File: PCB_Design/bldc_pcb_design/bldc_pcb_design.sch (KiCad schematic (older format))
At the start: 50 parts, among them IC1 DRV8305NPHPR, J1 Conn_01x04_Female, SW1 BOOT, SW2 RESET, U1 ESP32-WROOM-32D, U2 AS5600-ASOT, U3 LM2672M-3.3, U4 CSD18532NQ5B, U5 CSD18532NQ5B, U6 CSD18532NQ5B, U7 CSD18532NQ5B, U8 CSD18532NQ5B, U9 CSD18532NQ5B

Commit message: [Temp sensor] Added DS18S20Z+ and modified schematics
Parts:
- added C? (x2): 0.1uF, symbol Device:C
- added C? (x3): 2.2nF, symbol Device:C
- added D? (x2): LED, symbol Device:LED
- added R?: 4.7k, symbol Device:R
- added R?: 5k, symbol Device:R
- added R?: 330, symbol Device:R
- added U?: DS18S20Z+, SOIC127P600X175-8N, symbol DS18S20Z_:DS18S20Z+
- C11, C13, C9: value 1uF -> 0.01uF
- C14: value 4.7uF Ceramic -> 4.7uF
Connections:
- net labels added: TEMP_DQ
- net labels removed: +3V3
- wire segments 236 -> 261
- no-connect marks 5 -> 16
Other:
- note added: "**Confirm Usage of \nIO 5, 12, and 15 \n"
- note added: "3.3V Input Power LED\n"
- note added: "5-V internal analog \nsupply regulator\nbypass capacitor"
- note added: "Connect VDD to GND for\nParasite Power Mode:\nDeriving Power from DQ\nData line"
- note added: "Connect with-> \n3.3V or 5V, 50-mA LDO; \n connect 1-µF to GND\nReference voltage; \n LDO disabled"
- note added: "DQ - 1 Wire Line \nCommunication Interface\n"
- note added: "DQ - External Pull-Up"
- note added: "DRV_DVDD: 3.3V \ninternal digital\nsupply regulator"
- note added: "DRV_VREG: Internal\namplifier reference \nvoltage and SDO pullup."
- note added: "DRV_nFAULT: Fault\nIndicator and LED"
- note added: "High Side MOSFET Drain"
- note added: "PVDD: Power Bypass \nCapacitor and LED"
- note added: "PWRGD: Power Good DRV_VREG \nand MCU watchdog fault \nindication and LED"
- note added: "SNP1, SN2 and SN3 are negative current sense \ninput pins for amplifers 1,2 and 3 respectively\n"
- note added: "SO1, SO2 and SO3 are current amplifier output pins"
- note added: "SP1, SP2 and SP3 are positive current sense\ninput pins for amplifers 1,2 and 3 respectively\n"
- note added: "Temperature Sensor (DS18S20Z+)"
- note added: "VDRAIN Should \nHave Low\nImpedance Path\nTo Drain Of The \nHigh-Side FETs"
- note removed: "5-V internal analog supply \nregulator bypass capacitor"
- note removed: "Additional Circuitry"
- note removed: "Connect with-> \n3.3V or 5V, 50-mA LDO; \n connect 1-µF to GND\nReference voltage; LDO disabled"
- note removed: "DRV_DVDD: 3.3V internal digital\nsupply regulator"
- note removed: "DRV_VREG: Internalamplifier \nreference voltage and SDO pullup."
- note removed: "DRV_nFAULT: Fault\nIndicator"
- note removed: "High Side MOSFET\nDrain"
- note removed: "PWRGD: Power Good\nDRV_VREG and MCU \nwatchdog fault \nindication"
- note removed: "Power Bypass \nCapacitor"
- note removed: "Power LED\n"
- note removed: "SNP1, SN2 and SN3 are\nnegative current sense input pins\nfor amplifers 1,2 and 3 respectively\n"
- note removed: "SO1, SO2 and SO3 are \ncurrent amplifier output pins\n"
- note removed: "SP1, SP2 and SP3 are \npositive current sense input pins\nfor amplifers 1,2 and 3 respectively\n"
- moved on the sheet: C14, C15, C16, C17, C18, C19, C20, C21, C24, D3, R6, R7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

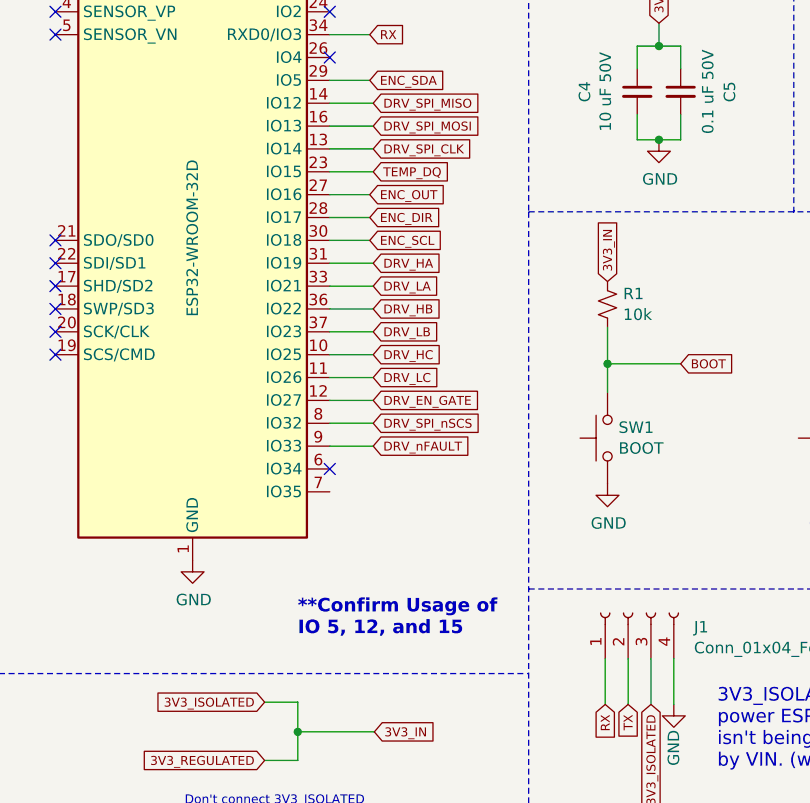
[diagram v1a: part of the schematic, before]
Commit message: Changed pin connections: IO34- DRV_nFAULT; IO15- NC; IO33- TEMP_DQ
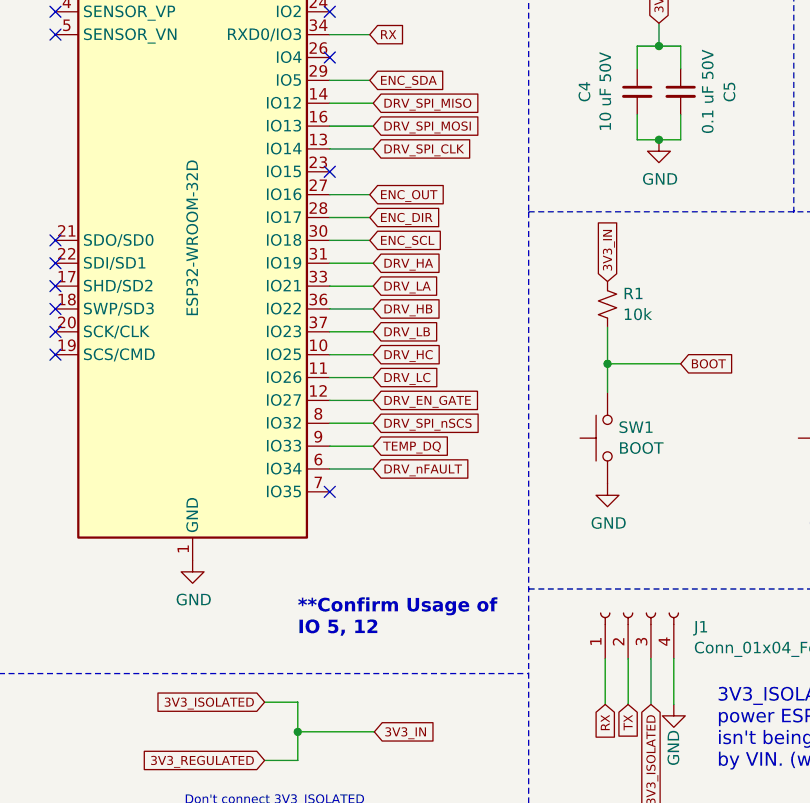
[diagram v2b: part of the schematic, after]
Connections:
- net DRV_nFAULT: now also U1.6 (IO34); no longer U1.9 (IO33)
- net TEMP_DQ: now also U1.9 (IO33); no longer U1.23 (IO15)
- no-connect marks 16 -> 17
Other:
- note added: "**Confirm Usage of \nIO 5, 12"
- note removed: "**Confirm Usage of \nIO 5, 12, and 15 \n"
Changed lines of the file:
@@
 Wire Wire Line
 	2290 2135 2100 2135
-Text GLabel 2290 3435 2    39   Input ~ 0
+Text GLabel 2290 3535 2    39   Input ~ 0
 DRV_nFAULT
 Text GLabel 2290 3135 2    39   Input ~ 0
@@
 	2290 3035 2100 3035
 Wire Wire Line
-	2290 3435 2100 3435
+	2290 3535 2100 3535
 Text GLabel 2290 2835 2    39   Input ~ 0
 DRV_HB
@@
 Wire Wire Line
 	8630 1155 8720 1155
-Text GLabel 2290 2235 2    39   Input ~ 0
+Text GLabel 2290 3435 2    39   Input ~ 0
 TEMP_DQ
 Wire Wire Line
-	2290 2235 2100 2235
+	2290 3435 2100 3435
 NoConn ~ 900  2535
 NoConn ~ 900  2635
@@
 NoConn ~ 2100 1735
 NoConn ~ 2100 1535
-NoConn ~ 2100 3535
+NoConn ~ 2100 3635
 $Comp
 L DS18S20Z_:DS18S20Z+ U?
@@
 	13770 3255 13770 2015
 Text Notes 1960 4270 0    59   ~ 12
-**Confirm Usage of \nIO 5, 12, and 15 \n
+**Confirm Usage of \nIO 5, 12
 Text GLabel 13565 4230 1    39   Input ~ 0
 SO1
@@
 Wire Notes Line
 	13445 3900 14320 3900
+NoConn ~ 2100 2235
 $EndSCHEMATC

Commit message: Optimised Schematics
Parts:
- added J?: XT30PW-M, XT30PWM, symbol XT30PW-M:XT30PW-M
- added R? (x3): 56, symbol Device:R
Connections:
- net POWER_IN is gone; now on net DRV_VREG: C6.1, U3.7 (VIN)
- net PVDD is gone; now on net DRV_VREG: C10.1, C11.1, C12.1, C13.1, C14.2, C18.2, C8.1, C9.1, D?.2 (A), IC1.41 (PVDD), R8.2, U4.5 (D), U4.6 (D), U4.7 (D), U4.8 (D), U6.5 (D), U6.6 (D), U6.7 (D), U6.8 (D), U8.5 (D), U8.6 (D), U8.7 (D), U8.8 (D)
- net SP1 is gone; now on net GND: C15.1, IC1.24 (SP1)
- net SP2 is gone; now on net GND: C16.1, IC1.22 (SP2)
- net SP3 is gone; now on net GND: C17.1, IC1.20 (SP3)
- net DRV_VREG: now also J?.2
- net GLA: now also U5.4 (G); no longer U5.1 (S)
- net GLB: now also U7.4 (G); no longer U7.1 (S), U9.1 (S)
- net GLC: now also U9.4 (G)
- net GND: now also J?.1, J?.3, J?.4
- net SLA: now also U5.1 (S); no longer U5.4 (G)
- net SLB: now also U7.1 (S); no longer U7.4 (G), U9.2 (S), U9.3 (S), U9.4 (G)
- net SLC: now also U9.1 (S), U9.2 (S), U9.3 (S)
- net SO1: now also R?.1
- net SO2: now also R?.1
- net SO3: now also R?.1
- net ISENB: now reaches U1.4 (SENSOR_VP)
- net ISENB: now also R?.2
- net ISENC: now reaches U1.5 (SENSOR_VN)
- net ISENC: now also R?.2
- net ISENA: now reaches U1.7 (IO35)
- net ISENA: now also R?.2
- no-connect marks 17 -> 14
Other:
- note added: "DRV_EN_GATE: Enables \ngate driver & current \nshunt amplifiers\n\nDVDD: 3.3V Internal\nVoltage Regulator\n\nAVDD: 5V Internal\nVoltage Regulator"
- note added: "LiPo Battery Connector"
- note added: "Operating Voltage for DRV8305 & MOSFETS:\n4.4 to 45 V (PVDD-Drain Voltage)\n"
- note added: "PVDD i.e input to the Driver\nand the board"
- note added: "Peak Gate Driver Current:\n1 to 1.25 A"
- note removed: "**Confirm Usage of \nIO 5, 12"
- moved on the sheet: C15, C16, C17, C19, C?, IC1

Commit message: Added Motor connector pads, rectified connections
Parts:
- added H1, H2, H3: MountingHole_Pad, symbol Mechanical:MountingHole_Pad
- R11, R13, R14: renamed from R?; value 56 -> 5m
- gave numbers to parts that had none: 12
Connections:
- net 3V3_IN: now also C19.2, D3.2 (A), D5.2 (A), IC1.48 (VREG), R6.1, R9.1
- net GND: now also C15.2, C16.2, C17.2; no longer C15.1, C16.1, C17.1
- net ISENA: now also C25.1
- net ISENB: now also C26.1
- net ISENC: now also C27.1
- net SLA: now also C15.1, IC1.23 (SN1)
- net SLB: now also C16.1, IC1.21 (SN2)
- net SLC: now also C17.1, IC1.19 (SN3)
- net SO1: no longer C26.1
- net SO2: no longer C25.1
- net SO3: no longer C27.1
- net DRV_VREG renamed POWER_IN
- net POWER_IN: no longer C19.2, D3.2 (A), D5.2 (A), IC1.48 (VREG), R6.1, R9.1
- net SHA renamed MOT_A
- net MOT_A: now also H1.1
- net SHB renamed MOT_B
- net MOT_B: now also H2.1
- net SHC renamed MOT_C
- net MOT_C: now also H3.1
- removed net SN1: C15.2, IC1.23 (SN1)
- removed net SN2: C16.2, IC1.21 (SN2)
- removed net SN3: C17.2, IC1.19 (SN3)
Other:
- note added: "Additional Circuitry"
- note added: "Motor Connector Pads"
- note added: "SN1, SN2 and SN3 are negative current sense \ninput pins for amplifers 1,2 and 3 respectively\n"
- note removed: "SNP1, SN2 and SN3 are negative current sense \ninput pins for amplifers 1,2 and 3 respectively\n"
- moved on the sheet: C15, C16, C17, C25, C26, C27, J2, R10, R11, R13, R14, U10

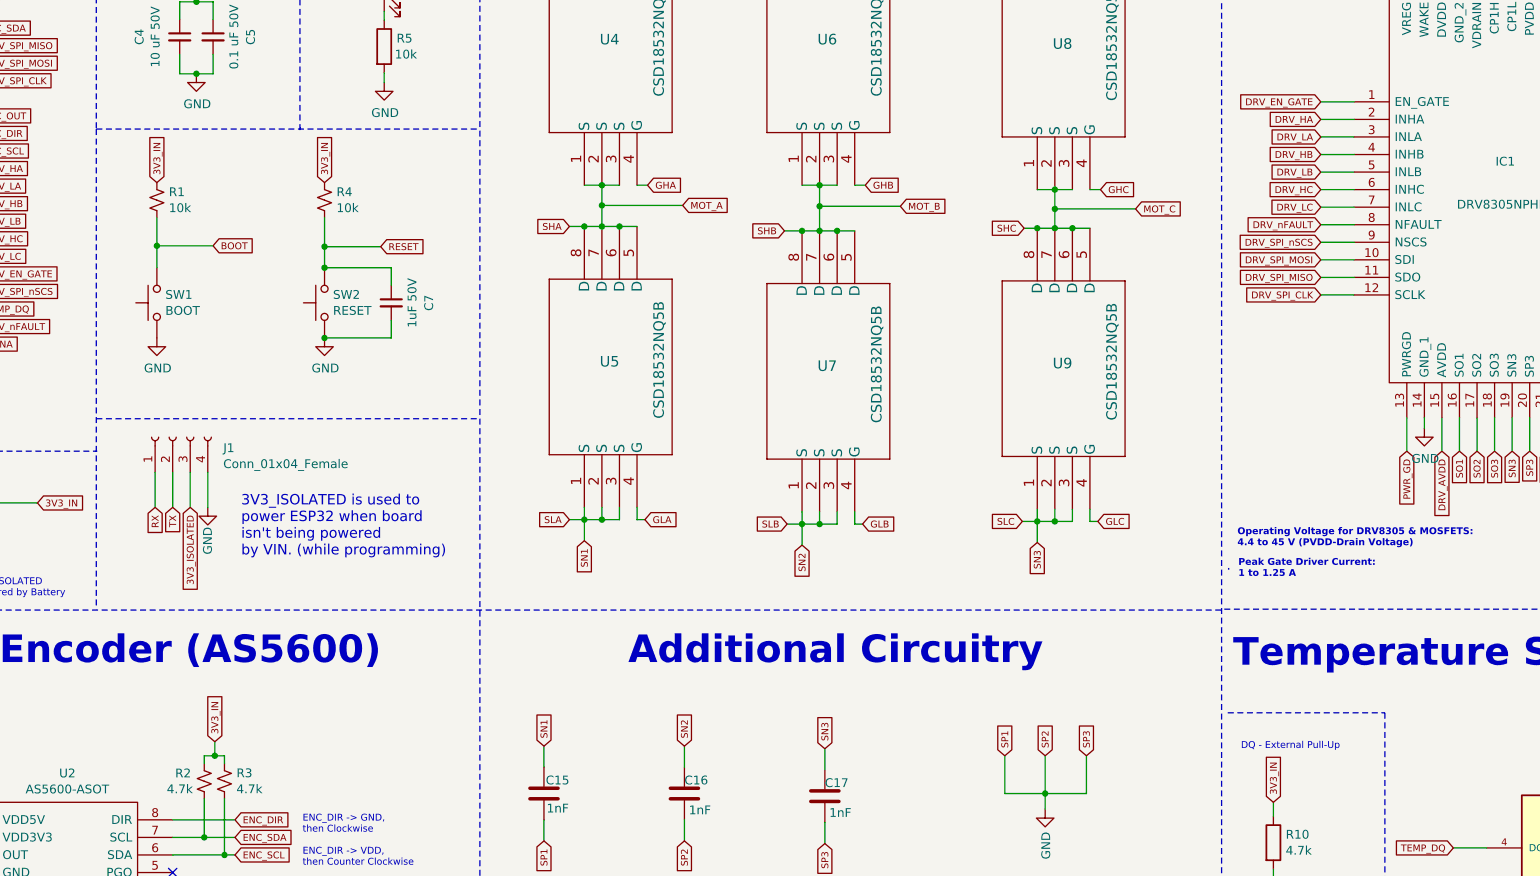
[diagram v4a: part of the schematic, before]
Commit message: Annotated components and assigned footprints
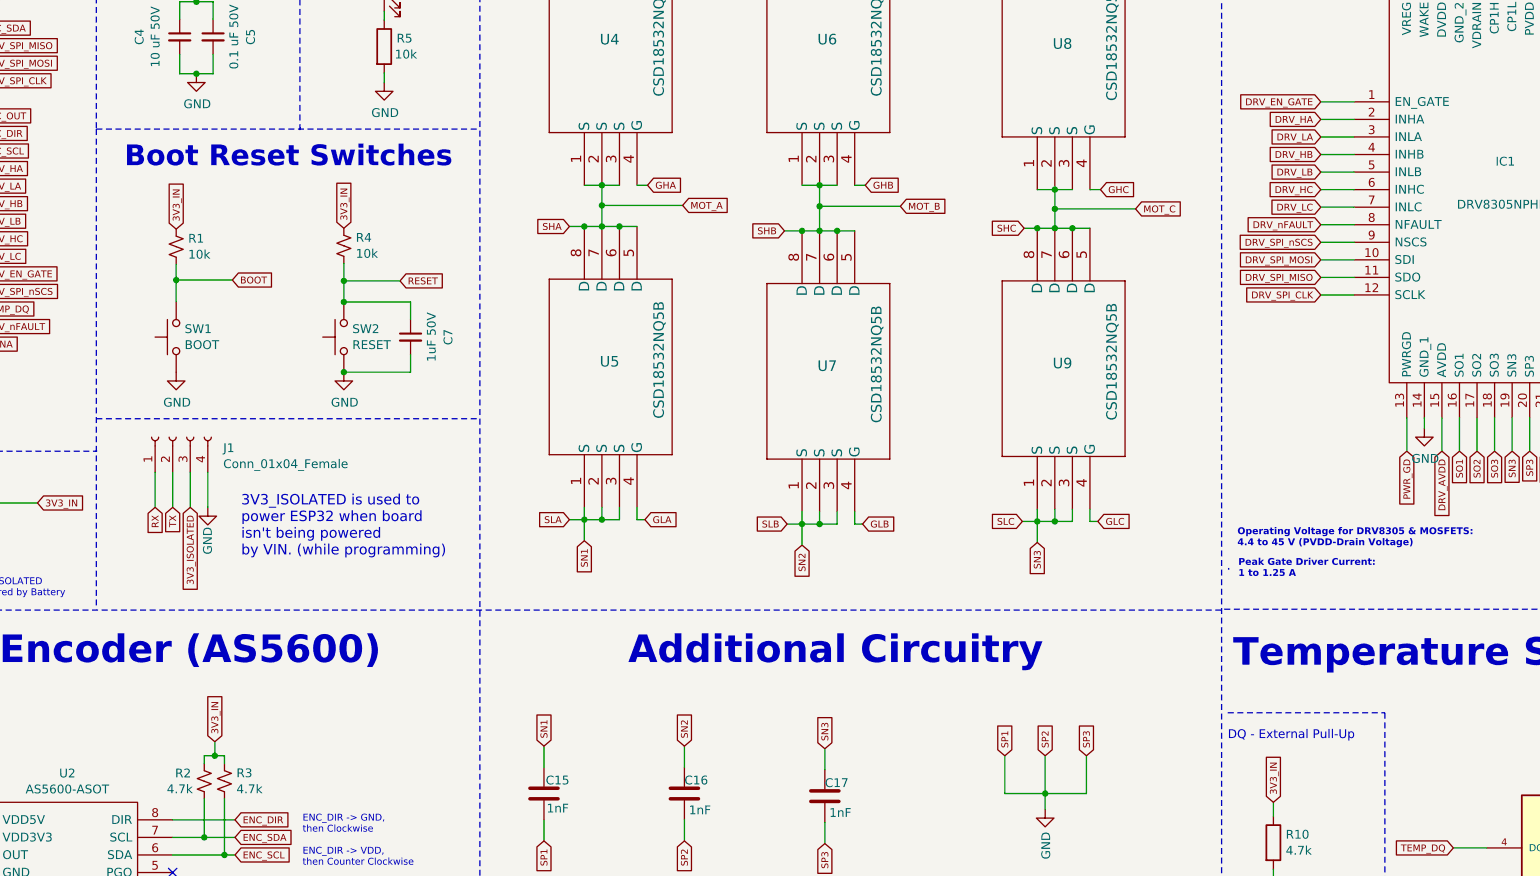
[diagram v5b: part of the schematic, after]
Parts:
- C1, C10, C11, C12, C13, C14, C15, C16, C17, C18, C19, C2, C20, C21, C22, C23, C24, C25, C26, C27, C28, C29, C3, C4, C5, C6, C7, C8, C9: footprint (none) -> Capacitor_SMD:C_0603_1608Metric
- D1, D2, D3, D4, D5: footprint (none) -> Diode_SMD:D_0603_1608Metric
- H1, H2, H3: footprint (none) -> MountingHole:MountingHole_2.7mm
- IC1: footprint QFP50P900X900X120-48N -> DRV8305NPHPR:DRV8305NPHPR
- J1: footprint (none) -> Connector_PinHeader_2.54mm:PinHeader_1x04_P2.54mm_Vertical
- J2: footprint XT30PWM -> XT30PW-M:XT30PWM
- L1: footprint (none) -> 8D43_Inductor:8D43
- R1, R10, R12, R15, R2, R3, R4, R5, R6, R7, R8, R9: footprint (none) -> Resistor_SMD:R_0603_1608Metric
- SW1, SW2: footprint (none) -> Tactile_Switch:Tactile_Switch
- U10: footprint SOIC127P600X175-8N -> DS18S20Z_:DS18S20Z_
- U2: footprint SOIC127P600X175-8N -> AS5600:AS5600
- U4, U5, U6, U7, U8, U9: footprint DNK8 -> CSD18532NQ5B:CSD18532NQ5B
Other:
- note added: "Boot Reset Switches"
- moved on the sheet: C7, R1, R4, SW1, SW2

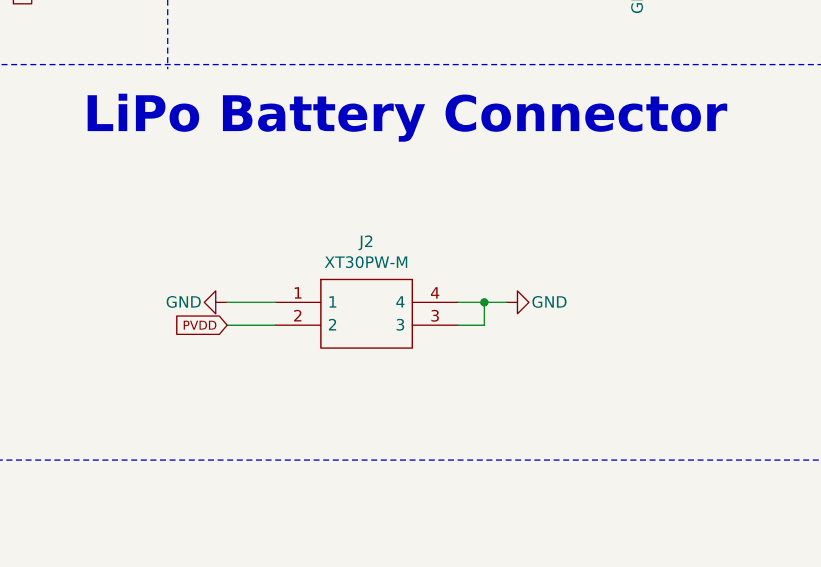
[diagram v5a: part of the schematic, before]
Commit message: Replaced Xt connector with motor pads
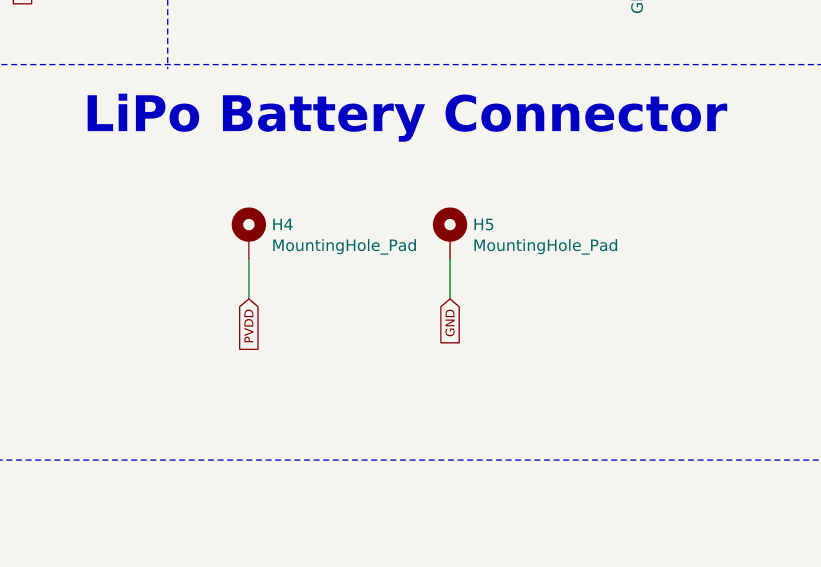
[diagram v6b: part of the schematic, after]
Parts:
- removed J2: XT30PW-M, XT30PW-M:XT30PWM, symbol XT30PW-M:XT30PW-M
- added H4, H5: MountingHole_Pad, MountingHole:MountingHole_6mm, symbol Mechanical:MountingHole_Pad
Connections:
- net GND: now also H5.1
- net POWER_IN: now also H4.1
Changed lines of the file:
@@
 Wire Wire Line
 	710  1635 900  1635
-$Comp
-L XT30PW-M:XT30PW-M J2
-U 1 1 6163DE2E
-P 10780 8445
-F 0 "J2" H 11180 8710 50  0000 C CNN
-F 1 "XT30PW-M" H 11180 8619 50  0000 C CNN
-F 2 "XT30PW-M:XT30PWM" H 11430 8545 50  0001 L CNN
-F 3 "https://www.tme.eu/sl/Document/ce4077e36b79046da520ca73227e15de/XT30PW%20SPEC.pdf" H 11430 8445 50  0001 L CNN
-F 4 "30A Low Temperature Rise Fire Retardant Plug" H 11430 8345 50  0001 L CNN "Description"
-F 5 "5" H 11430 8245 50  0001 L CNN "Height"
-F 6 "Amass" H 11430 8145 50  0001 L CNN "Manufacturer_Name"
-F 7 "XT30PW-M" H 11430 8045 50  0001 L CNN "Manufacturer_Part_Number"
-F 8 "" H 11430 7945 50  0001 L CNN "Mouser Part Number"
-F 9 "" H 11430 7845 50  0001 L CNN "Mouser Price/Stock"
-F 10 "" H 11430 7745 50  0001 L CNN "Arrow Part Number"
-F 11 "" H 11430 7645 50  0001 L CNN "Arrow Price/Stock"
-	1    10780 8445
-	1    0    0    -1
-$EndComp
 Text Notes 9940 7725 0    157  ~ 31
 LiPo Battery Connector
@@
 Text Notes 570  5050 0    39   ~ 0
 PVDD i.e input to the Driver\nand the board
-$Comp
-L power:GND #PWR024
-U 1 1 618A58D3
-P 10570 8445
-F 0 "#PWR024" H 10570 8195 50  0001 C CNN
-F 1 "GND" V 10570 8255 50  0000 C CNN
-F 2 "" H 10570 8445 50  0001 C CNN
-F 3 "" H 10570 8445 50  0001 C CNN
-	1    10570 8445
-	0    1    1    0
-$EndComp
-Wire Wire Line
-	10780 8445 10570 8445
-$Comp
-L power:GND #PWR025
-U 1 1 618E84E4
-P 11790 8445
-F 0 "#PWR025" H 11790 8195 50  0001 C CNN
-F 1 "GND" V 11790 8255 50  0000 C CNN
-F 2 "" H 11790 8445 50  0001 C CNN
-F 3 "" H 11790 8445 50  0001 C CNN
-	1    11790 8445
-	0    -1   -1   0
-$EndComp
-Wire Wire Line
-	11580 8445 11695 8445
-Wire Wire Line
-	11580 8545 11695 8545
-Wire Wire Line
-	11695 8545 11695 8445
-Connection ~ 11695 8445
-Wire Wire Line
-	11695 8445 11790 8445
-Wire Wire Line
-	10780 8545 10570 8545
-Text GLabel 10570 8545 0    39   Input ~ 0
-PVDD
 Text GLabel 13160 2660 0    39   Input ~ 0
 3V3_IN
@@
 Text Notes 3130 2640 0    118  ~ 24
 Boot Reset Switches
+Wire Wire Line
+	11545 8255 11545 8430
+Text GLabel 11545 8430 3    39   Input ~ 0
+GND
+$Comp
+L Mechanical:MountingHole_Pad H5
+U 1 1 61833E09
+P 11545 8155
+F 0 "H5" H 11645 8204 50  0000 L CNN
+F 1 "MountingHole_Pad" H 11645 8113 50  0000 L CNN
+F 2 "MountingHole:MountingHole_6mm" H 11545 8155 50  0001 C CNN
+F 3 "~" H 11545 8155 50  0001 C CNN
+	1    11545 8155
+	1    0    0    -1
+$EndComp
+Wire Wire Line
+	10665 8255 10665 8430
+Text GLabel 10665 8430 3    39   Input ~ 0
+PVDD
+$Comp
+L Mechanical:MountingHole_Pad H4
+U 1 1 61833E01
+P 10665 8155
+F 0 "H4" H 10765 8204 50  0000 L CNN
+F 1 "MountingHole_Pad" H 10765 8113 50  0000 L CNN
+F 2 "MountingHole:MountingHole_6mm" H 10665 8155 50  0001 C CNN
+F 3 "~" H 10665 8155 50  0001 C CNN
+	1    10665 8155
+	1    0    0    -1
+$EndComp
 $EndSCHEMATC
